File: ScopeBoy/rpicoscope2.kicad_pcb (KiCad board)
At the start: 4 copper layers, 100 x 80 mm, 79 parts, among them J1 Conn_01x02, J2 Conn_01x02_Male, J3 Conn_01x05, J4 Conn_01x10, J5 Conn_01x04, U1 LP2985-3.3, U10 LM4040DBZ-2.0, U11 TLV3501, U12 DAC5571, U13 TLV271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

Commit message: Initial version of the PCB done
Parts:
- added J6: Conn_01x03, Connector_JST:JST_SH_SM03B-SRSS-TB_1x03-1MP_P1.00mm_Horizontal, F.Cu at (132.0, 123.8)
- added J7: Conn_01x03, Connector_JST:JST_SH_SM03B-SRSS-TB_1x03-1MP_P1.00mm_Horizontal, F.Cu at (132.0, 133.6)
- added J8: Conn_01x02, Connector_JST:JST_PH_S2B-PH-SM4-TB_1x02-1MP_P2.00mm_Horizontal, F.Cu at (212.8, 90.7)
- moved J3 53.1 mm to (156.7, 78.2)
- moved J5 21.6 mm to (154.7, 137.3), turned to 90 degrees
- moved J1 0.56 mm to (123.3, 109.8)
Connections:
- U9 pad 11: SEL0 -> TX
- U9 pad 12: SEL1 -> RX
- U9 pad 14: unconnected-(U9-GP10-Pad14) -> SEL0
- U9 pad 15: ROTSW -> SEL1
- U9 pad 32: SEL -> ROTSW
- U9 pad 41: unconnected-(U9-SWCLK-Pad41) -> SWCLK
- U9 pad 43: unconnected-(U9-SWIO-Pad43) -> SWIO
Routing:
- net +3V3Pico: track 0.00 -> 163.0 mm, vias 0 -> 4
- net SEL1: track 0.00 -> 131.2 mm
- net RX: track 0.00 -> 126.8 mm, vias 0 -> 2
- net TX: track 0.00 -> 121.7 mm, vias 0 -> 2
- net SEL0: track 0.00 -> 108.5 mm, vias 0 -> 2
- net ROTSW: track 0.00 -> 91.5 mm, vias 0 -> 2
- net GND: track 239.2 -> 328.6 mm, vias 11 -> 16
- net SCL: track 64.6 -> 146.3 mm, vias 3 -> 4
- net SDA: track 66.1 -> 147.2 mm, vias 3 -> 6
- net SWIO: track 0.00 -> 69.4 mm, vias 0 -> 2
- net SDCS: track 0.00 -> 69.2 mm
- net +5V: track 242.0 -> 175.7 mm
- net SWCLK: track 0.00 -> 65.3 mm, vias 0 -> 2
- net ROTDT: track 0.00 -> 55.3 mm, vias 0 -> 2
- net BACKLIGHT: track 0.00 -> 53.3 mm
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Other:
- board text added: "SWD"
- board text added: "ScopeBoy Original Design by Jenny List Modified by Robbie Leslie ECE 5730 Cornell University 2025"
- board text added: "UART"

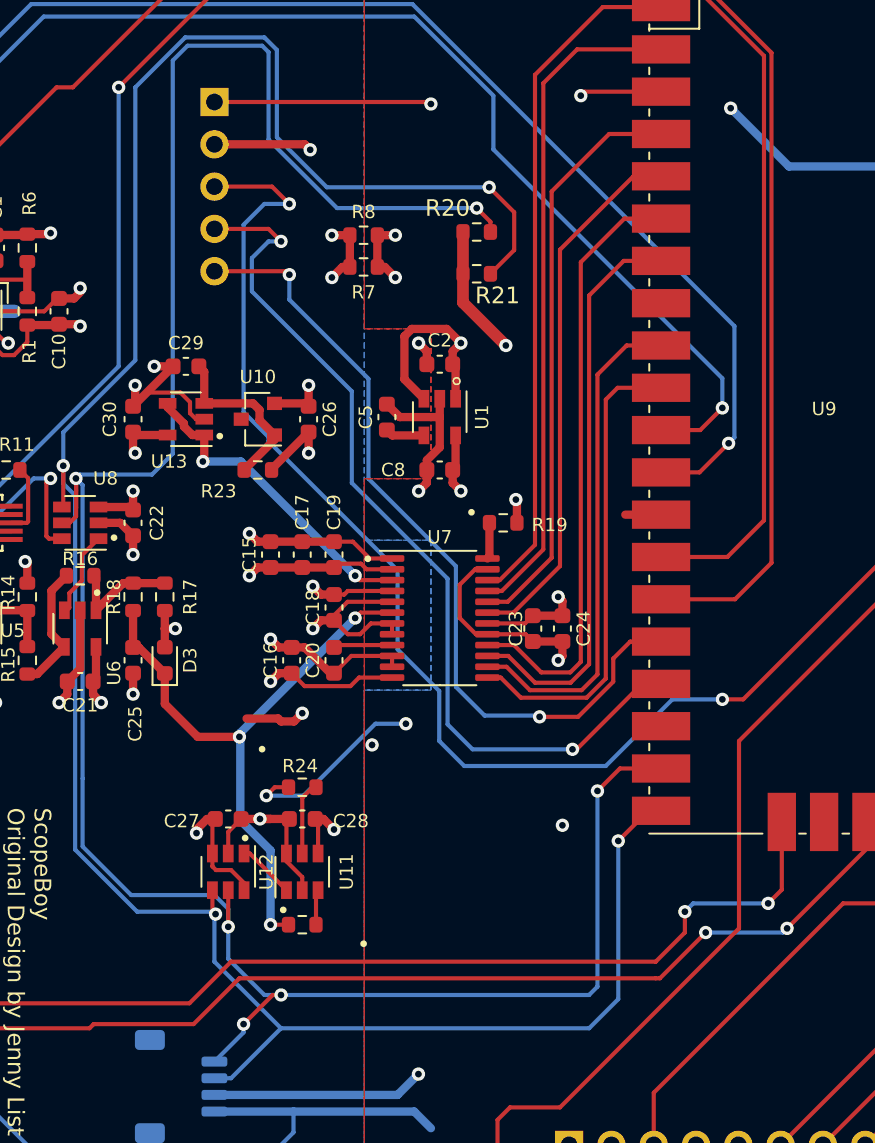
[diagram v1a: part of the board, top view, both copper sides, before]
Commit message: Added caps on encoder
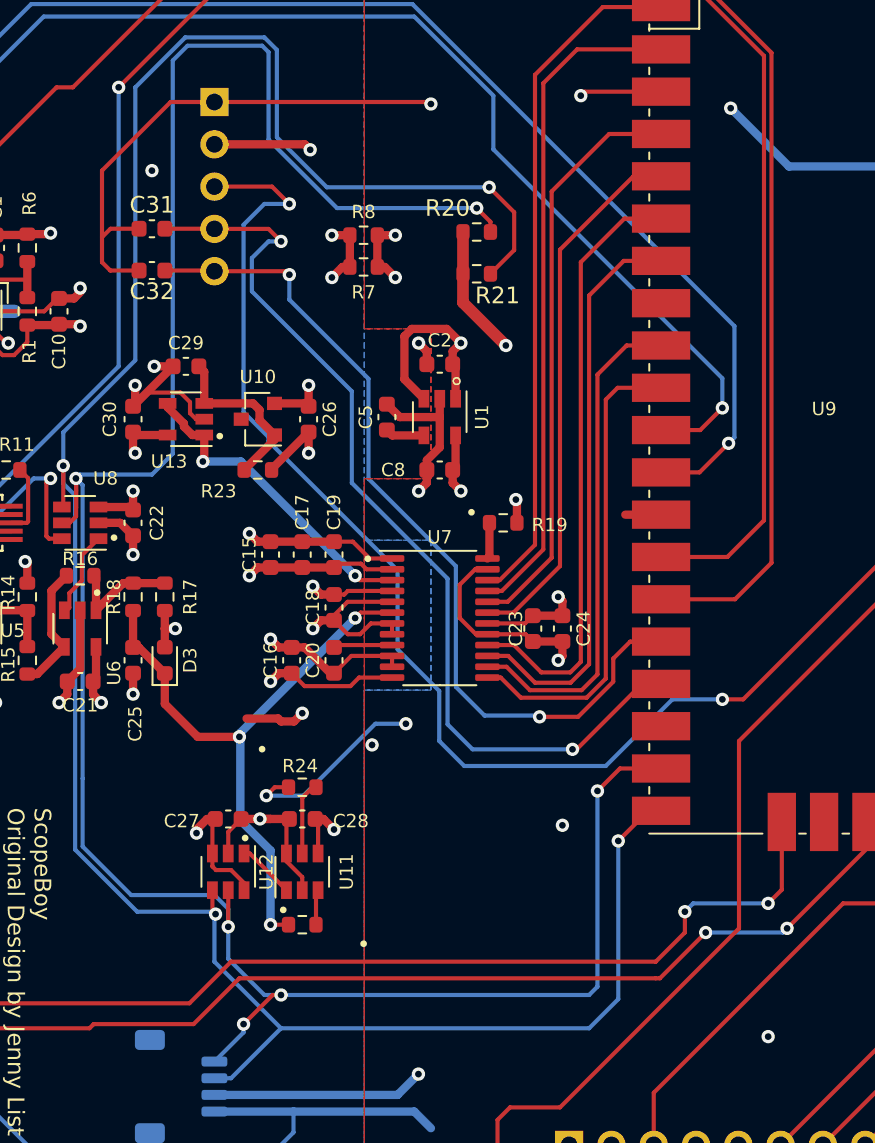
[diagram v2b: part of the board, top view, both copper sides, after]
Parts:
- added C31: 10nF, Capacitor_SMD:C_0603_1608Metric, F.Cu at (152.9, 85.8)
- added C32: 10nF, Capacitor_SMD:C_0603_1608Metric, F.Cu at (152.9, 88.3)
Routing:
- net GND: track 328.6 -> 347.4 mm, vias 16 -> 17
- net ROTCLK: track 50.1 -> 53.1 mm
- net ROTDT: track 55.3 -> 58.3 mm
- net GNDA: vias 25 -> 26

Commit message: Final revision of PCB. Updated some components
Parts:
- added Q1: Q_PMOS_GSD, Package_TO_SOT_SMD:SOT-23-3, F.Cu at (212.3, 86.2)
- J8: footprint Connector_JST:JST_PH_S2B-PH-SM4-TB_1x02-1MP_P2.00mm_Horizontal -> Connector_PinHeader_2.54mm:PinHeader_1x02_P2.54mm_Vertical; moved to B.Cu
- moved J8 92.5 mm to (134.4, 139.8), turned to 180 degrees
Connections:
- C1 pad 1: +5V -> VSYS
- C2 pad 2: +5V -> VSYS
- J8 pad 1: +5V -> Net-(J8-Pin_1)
- U1 pad 1: +5V -> VSYS
- U1 pad 3: +5V -> VSYS
- U2 pad 12: +5V -> VSYS
- U2 pad 3: +5V -> VSYS
- U2 pad 8: +5V -> VSYS
- U9 pad 39: unconnected-(U9-VSYS-Pad39) -> VSYS
- U9 pad 40: +5V -> VBUS
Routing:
- net +5V: track 175.7 -> 0.00 mm, vias 8 -> 0
- net VSYS: track 0.00 -> 167.1 mm, vias 0 -> 8
- net Net-(J8-Pin_1): track 0.00 -> 137.9 mm
- net VBUS: track 0.00 -> 20.0 mm
- net GND: track 347.4 -> 353.8 mm
- added copper zone on In2.Cu, net VSYS
- removed copper zone on In2.Cu, net +5V
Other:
- board text added: "Battery Charger"
- board text added: "Joystick"
- board text added: "Rotary"
- board text added: "TFT"

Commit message: Quick cap replacement (same footprint)
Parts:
- J5: value Conn_01x04 -> SM04B-SRSS-TB
- J6, J7: value Conn_01x03 -> SM03B-SRSS-TB
- Q1: value Q_PMOS_GSD -> DMG2305UX-7
- U3: value TPH2501 -> OPA354
